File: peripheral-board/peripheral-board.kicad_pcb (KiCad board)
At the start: 2 copper layers, 165 x 100 mm, 144 parts, among them IC1001 ATTINY48-A, SW2001 1, SW2002 2, SW2003 3, SW2004 4, SW2005 5, SW2006 6, SW2007 7, SW2008 8, SW2009 9, SW2010 0, SW2011 1, SW2012 2, SW2013 3, SW2014 4, SW2015 5, SW2016 6, SW2017 7, SW2018 8, SW2019 9, SW2020 0, SW2021 Q, SW2022 W, SW2023 E, SW2024 R, SW2025 T, SW2026 Y, SW2027 U, SW2028 I, SW2029 O, SW2030 P, SW2031 Q, SW2032 W, SW2033 E, SW2034 R, SW2035 T, SW2036 Y, SW2037 U, SW2038 I, SW2039 O, SW2040 P, SW2041 A, SW2042 S, SW2043 D, SW2044 F, SW2045 G, SW2046 H, SW2047 J, SW2048 K, SW2049 L, SW2050 Ö, SW2051 A, SW2052 S, SW2053 D, SW2054 F, SW2055 G, SW2056 H, SW2057 J, SW2058 K, SW2059 L, SW2060 Ö, SW2061 Z, SW2062 X, SW2063 C, SW2064 V, SW2065 B, SW2066 N, SW2067 M, SW2068 ,, SW2069 ., SW2070 -, SW3001 Left, SW3002 MIddle, SW3003 Right

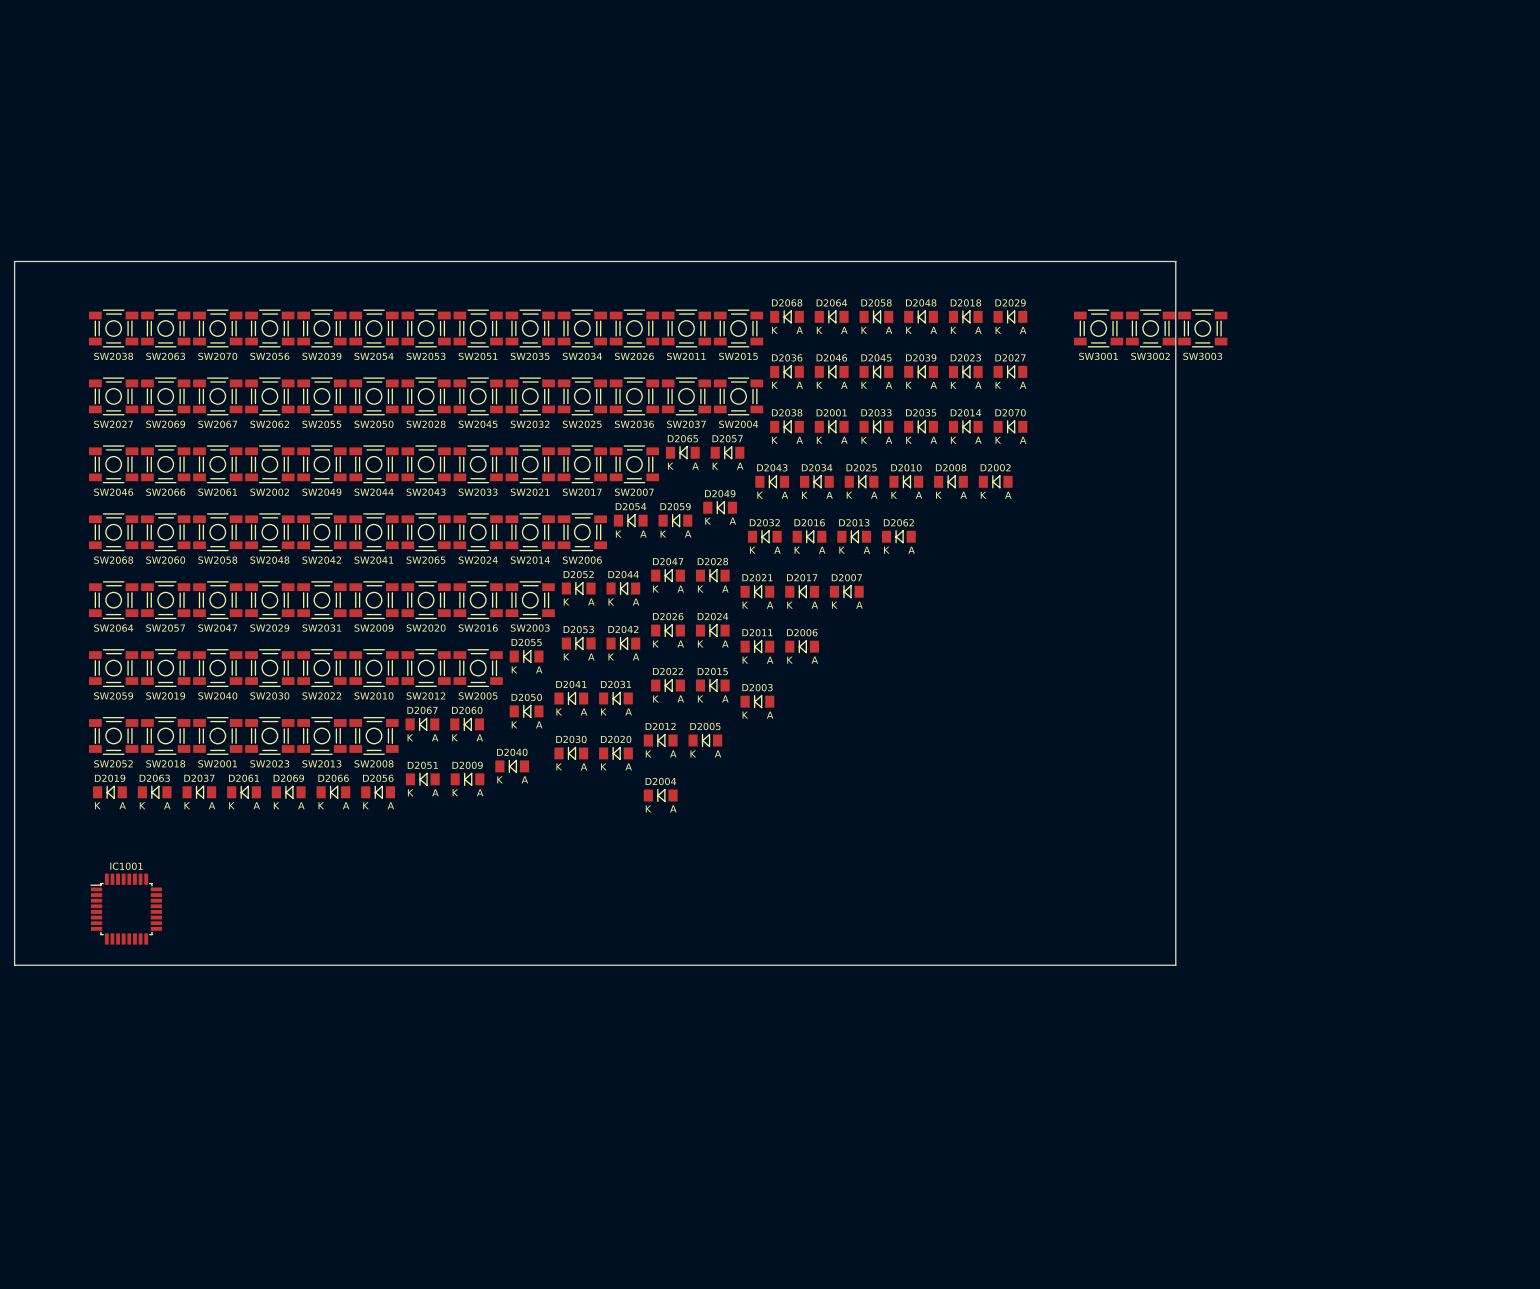
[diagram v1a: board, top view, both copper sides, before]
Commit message: added keyboard scanning logic
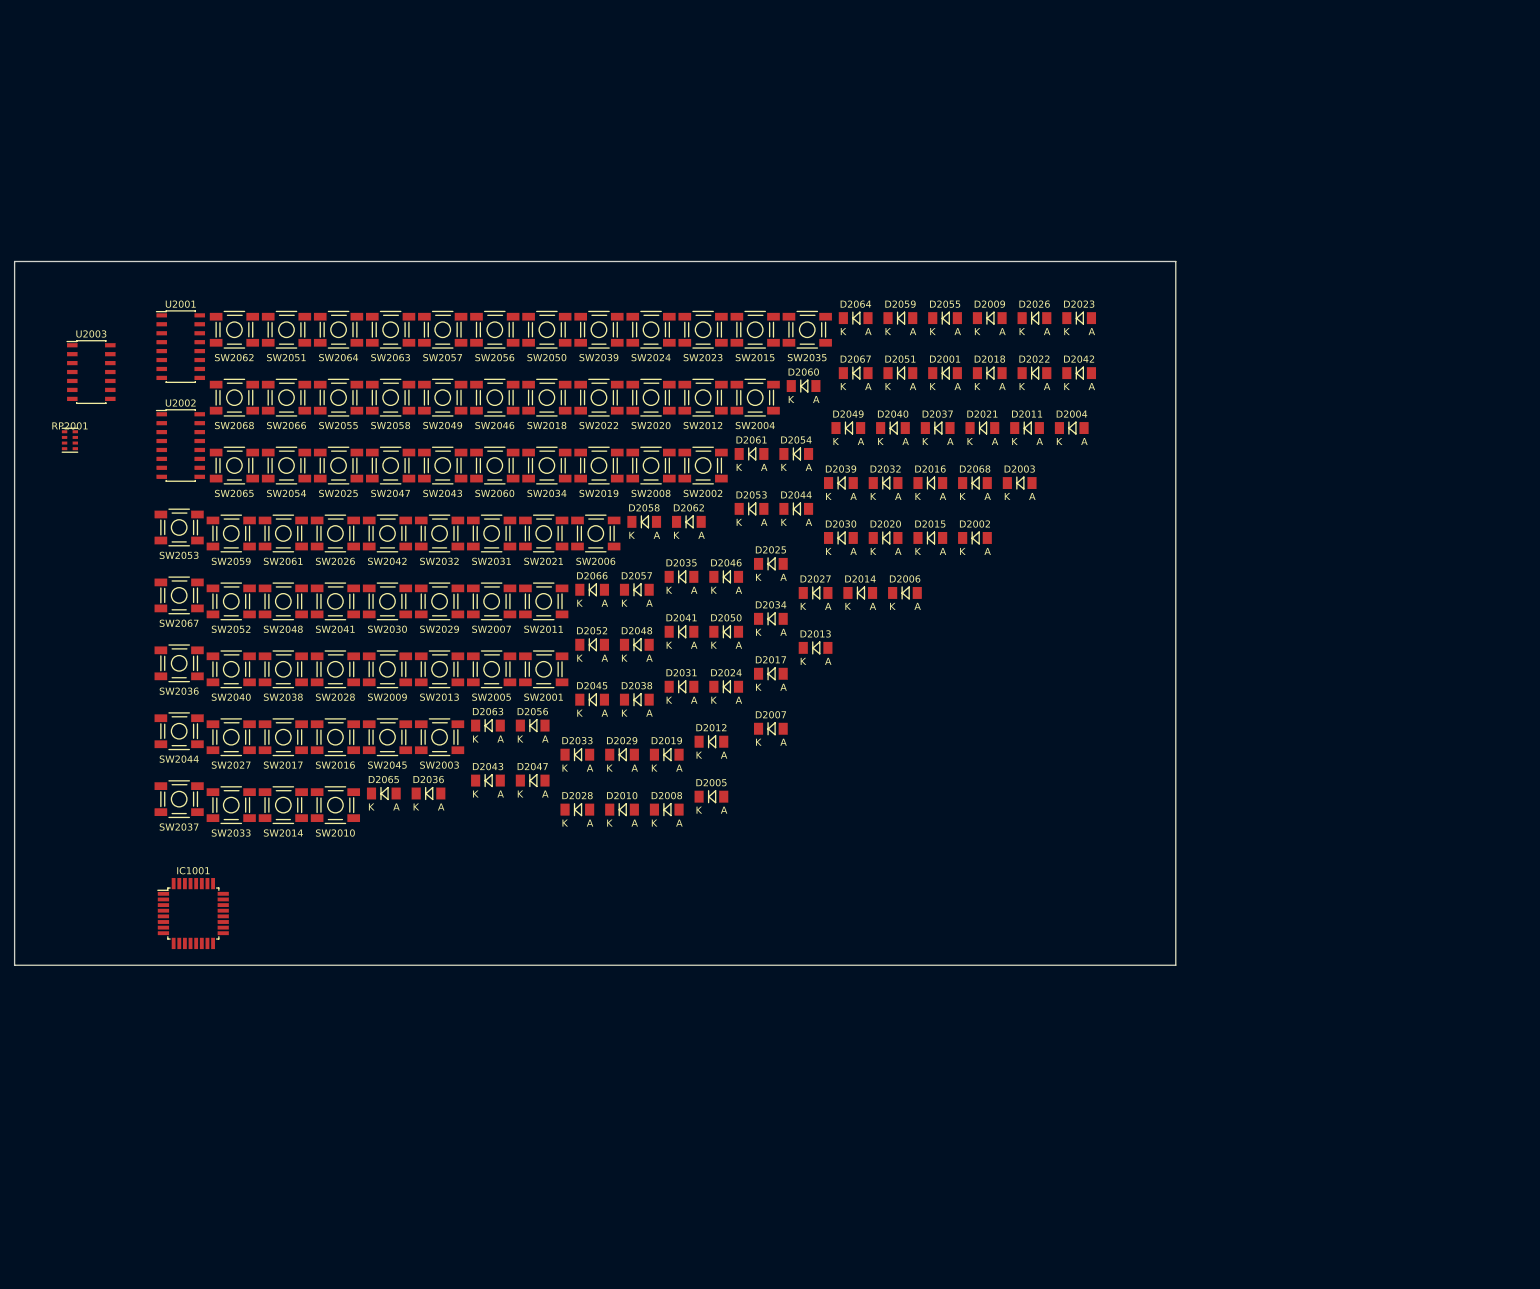
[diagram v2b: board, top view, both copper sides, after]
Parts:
- removed D2069, D2070: 1N4148, Diodes_SMD:MiniMELF_Standard
- removed SW2069: ., lib:SMD-TACT-5.2x5.2x2mm
- removed SW2070: -, lib:SMD-TACT-5.2x5.2x2mm
- removed SW3001: Left, lib:SMD-TACT-5.2x5.2x2mm
- removed SW3002: MIddle, lib:SMD-TACT-5.2x5.2x2mm
- removed SW3003: Right, lib:SMD-TACT-5.2x5.2x2mm
- added RP2001: 10k, Resistors_SMD:R_Cat16-4, F.Cu at (67.9, 70.4)
- added U2001: 4017, Housings_SOIC:SOIC-16_3.9x9.9mm_Pitch1.27mm, F.Cu at (83.6, 57.1)
- added U2002: 4017, Housings_SOIC:SOIC-16_3.9x9.9mm_Pitch1.27mm, F.Cu at (83.6, 71.1)
- added U2003: 74HC00, Housings_SOIC:SOIC-14_3.9x8.7mm_Pitch1.27mm, F.Cu at (70.9, 60.7)
- SW2011: value 1 -> +
- SW2012: value 2 -> ´
- SW2013: value 3 -> BKSP
- SW2014: value 4 -> TROLL
- SW2015: value 5 -> §
- SW2016: value 6 -> UP
- SW2017: value 7 -> RMB
- SW2018: value 8 -> Q
- SW2019: value 9 -> W
- SW2020: value 0 -> E
- SW2021: value Q -> R
- SW2022: value W -> T
- SW2023: value E -> Y
- SW2024: value R -> U
- SW2025: value T -> I
- SW2026: value Y -> O
- SW2027: value U -> P
- SW2028: value I -> Å
- SW2029: value O -> ¨
- SW2030: value P -> RETURN
- SW2031: value Q -> ALT_GR
- SW2032: value W -> <
- SW2033: value E -> LEFT
- SW2034: value R -> MMB
- SW2035: value T -> A
- SW2036: value Y -> S
- SW2037: value U -> D
- SW2038: value I -> F
- SW2039: value O -> G
- SW2040: value P -> H
- SW2041: value A -> J
- SW2042: value S -> K
- SW2043: value D -> L
- SW2044: value F -> Ö
- SW2045: value G -> Ä
- SW2046: value H -> '
- SW2047: value J -> ESC
- SW2048: value K -> TAB
- SW2049: value L -> ALT
- SW2050: value Ö -> DOWN
- SW2051: value A -> LMB
- SW2052: value S -> SHIFT_L
- SW2053: value D -> Z
- SW2054: value F -> X
- SW2055: value G -> C
- SW2056: value H -> V
- SW2057: value J -> B
- SW2058: value K -> N
- SW2059: value L -> M
- SW2060: value Ö -> ,
- SW2061: value Z -> .
- SW2062: value X -> -
- SW2063: value C -> SHIFT_R
- SW2064: value V -> FN_R
- SW2065: value B -> SPACE
- SW2066: value N -> FN_L
- SW2067: value M -> RIGHT
- SW2068: value , -> CTRL
- moved D2037 117.0 mm to (191.2, 68.7)
- moved D2009 99.0 mm to (198.6, 53.0)
- moved SW2037 92.0 mm to (83.4, 121.4)
- moved D2051 89.1 mm to (185.9, 60.9)
- moved D2061 86.7 mm to (164.7, 72.3)
- moved SW2023 84.4 mm to (157.8, 54.7)
- moved D2029 83.2 mm to (146.3, 115.1)
- moved D2019 79.3 mm to (152.7, 115.1)
- moved D2067 79.3 mm to (179.5, 60.9)
- moved D2036 78.6 mm to (118.8, 120.6)
- moved D2004 78.3 mm to (210.2, 68.7)
- moved D2055 76.5 mm to (192.2, 53.0)
- moved D2042 75.3 mm to (211.3, 60.9)
- moved SW2036 75.0 mm to (83.4, 102.1)
- moved SW2018 72.4 mm to (135.6, 64.3)
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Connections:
- D2001 pad 1: Net-(D2001-Pad1) -> /Keyboard/Q0
- D2002 pad 1: Net-(D2001-Pad1) -> /Keyboard/Q0
- D2003 pad 1: Net-(D2001-Pad1) -> /Keyboard/Q0
- D2004 pad 1: Net-(D2001-Pad1) -> /Keyboard/Q0
- D2005 pad 1: Net-(D2001-Pad1) -> /Keyboard/Q0
- D2006 pad 1: Net-(D2001-Pad1) -> /Keyboard/Q0
- D2007 pad 1: Net-(D2001-Pad1) -> /Keyboard/Q0
- D2008 pad 1: Net-(D2001-Pad1) -> /Keyboard/Q0
- D2009 pad 1: Net-(D2001-Pad1) -> /Keyboard/Q0
- D2010 pad 1: Net-(D2001-Pad1) -> /Keyboard/Q0
- D2011 pad 1: Net-(D2011-Pad1) -> /Keyboard/Q0
- D2012 pad 1: Net-(D2011-Pad1) -> /Keyboard/Q0
- D2013 pad 1: Net-(D2011-Pad1) -> /Keyboard/Q0
- D2014 pad 1: Net-(D2011-Pad1) -> /Keyboard/Q0
- D2015 pad 1: Net-(D2011-Pad1) -> /Keyboard/Q0
- D2016 pad 1: Net-(D2011-Pad1) -> /Keyboard/Q0
- D2017 pad 1: Net-(D2011-Pad1) -> /Keyboard/Q0
- D2018 pad 1: Net-(D2011-Pad1) -> /Keyboard/Q1
- D2019 pad 1: Net-(D2011-Pad1) -> /Keyboard/Q1
- D2020 pad 1: Net-(D2011-Pad1) -> /Keyboard/Q1
- D2021 pad 1: Net-(D2021-Pad1) -> /Keyboard/Q1
- D2022 pad 1: Net-(D2021-Pad1) -> /Keyboard/Q1
- D2023 pad 1: Net-(D2021-Pad1) -> /Keyboard/Q1
- D2024 pad 1: Net-(D2021-Pad1) -> /Keyboard/Q1
- D2025 pad 1: Net-(D2021-Pad1) -> /Keyboard/Q1
- D2026 pad 1: Net-(D2021-Pad1) -> /Keyboard/Q1
- D2027 pad 1: Net-(D2021-Pad1) -> /Keyboard/Q1
- D2028 pad 1: Net-(D2021-Pad1) -> /Keyboard/Q1
- D2029 pad 1: Net-(D2021-Pad1) -> /Keyboard/Q1
- D2030 pad 1: Net-(D2021-Pad1) -> /Keyboard/Q1
- D2031 pad 1: Net-(D2031-Pad1) -> /Keyboard/Q1
- D2032 pad 1: Net-(D2031-Pad1) -> /Keyboard/Q1
- D2033 pad 1: Net-(D2031-Pad1) -> /Keyboard/Q1
- D2034 pad 1: Net-(D2031-Pad1) -> /Keyboard/Q1
- D2035 pad 1: Net-(D2031-Pad1) -> /Keyboard/Q2
- D2036 pad 1: Net-(D2031-Pad1) -> /Keyboard/Q2
- D2037 pad 1: Net-(D2031-Pad1) -> /Keyboard/Q2
- D2038 pad 1: Net-(D2031-Pad1) -> /Keyboard/Q2
- D2039 pad 1: Net-(D2031-Pad1) -> /Keyboard/Q2
- D2040 pad 1: Net-(D2031-Pad1) -> /Keyboard/Q2
- D2041 pad 1: Net-(D2041-Pad1) -> /Keyboard/Q2
- D2042 pad 1: Net-(D2041-Pad1) -> /Keyboard/Q2
- D2043 pad 1: Net-(D2041-Pad1) -> /Keyboard/Q2
- D2044 pad 1: Net-(D2041-Pad1) -> /Keyboard/Q2
- D2045 pad 1: Net-(D2041-Pad1) -> /Keyboard/Q2
- D2046 pad 1: Net-(D2041-Pad1) -> /Keyboard/Q2
- D2047 pad 1: Net-(D2041-Pad1) -> /Keyboard/Q2
- D2048 pad 1: Net-(D2041-Pad1) -> /Keyboard/Q2
- D2049 pad 1: Net-(D2041-Pad1) -> /Keyboard/Q2
- D2050 pad 1: Net-(D2041-Pad1) -> /Keyboard/Q2
- D2051 pad 1: Net-(D2051-Pad1) -> /Keyboard/Q2
- D2052 pad 1: Net-(D2051-Pad1) -> /Keyboard/Q3
- D2053 pad 1: Net-(D2051-Pad1) -> /Keyboard/Q3
- D2054 pad 1: Net-(D2051-Pad1) -> /Keyboard/Q3
- D2055 pad 1: Net-(D2051-Pad1) -> /Keyboard/Q3
- D2056 pad 1: Net-(D2051-Pad1) -> /Keyboard/Q3
- D2057 pad 1: Net-(D2051-Pad1) -> /Keyboard/Q3
- D2058 pad 1: Net-(D2051-Pad1) -> /Keyboard/Q3
- D2059 pad 1: Net-(D2051-Pad1) -> /Keyboard/Q3
- D2060 pad 1: Net-(D2051-Pad1) -> /Keyboard/Q3
- D2061 pad 1: Net-(D2061-Pad1) -> /Keyboard/Q3
- D2062 pad 1: Net-(D2061-Pad1) -> /Keyboard/Q3
- D2063 pad 1: Net-(D2061-Pad1) -> /Keyboard/Q3
- D2064 pad 1: Net-(D2061-Pad1) -> /Keyboard/Q3
- D2065 pad 1: Net-(D2061-Pad1) -> /Keyboard/Q3
- D2066 pad 1: Net-(D2061-Pad1) -> /Keyboard/Q3
- D2067 pad 1: Net-(D2061-Pad1) -> /Keyboard/Q3
- D2068 pad 1: Net-(D2061-Pad1) -> /Keyboard/Q3
- SW2018 pad 1: Net-(SW2018-Pad1) -> Net-(SW2001-Pad1)
- SW2019 pad 1: Net-(SW2019-Pad1) -> Net-(SW2002-Pad1)
- SW2020 pad 1: Net-(SW2020-Pad1) -> Net-(SW2003-Pad1)
- SW2021 pad 1: Net-(SW2001-Pad1) -> Net-(SW2004-Pad1)
- SW2022 pad 1: Net-(SW2002-Pad1) -> Net-(SW2005-Pad1)
- SW2023 pad 1: Net-(SW2003-Pad1) -> Net-(SW2006-Pad1)
- SW2024 pad 1: Net-(SW2004-Pad1) -> Net-(SW2007-Pad1)
- SW2025 pad 1: Net-(SW2005-Pad1) -> Net-(SW2008-Pad1)
- SW2026 pad 1: Net-(SW2006-Pad1) -> Net-(SW2009-Pad1)
- SW2027 pad 1: Net-(SW2007-Pad1) -> Net-(SW2010-Pad1)
- SW2028 pad 1: Net-(SW2008-Pad1) -> Net-(SW2011-Pad1)
- SW2029 pad 1: Net-(SW2029-Pad1) -> Net-(SW2012-Pad1)
- SW2030 pad 1: Net-(SW2010-Pad1) -> Net-(SW2013-Pad1)
- SW2031 pad 1: Net-(SW2011-Pad1) -> Net-(SW2014-Pad1)
- SW2032 pad 1: Net-(SW2012-Pad1) -> Net-(SW2015-Pad1)
- SW2033 pad 1: Net-(SW2013-Pad1) -> Net-(SW2016-Pad1)
- SW2034 pad 1: Net-(SW2014-Pad1) -> Net-(SW2017-Pad1)
- SW2035 pad 1: Net-(SW2015-Pad1) -> Net-(SW2001-Pad1)
- SW2036 pad 1: Net-(SW2016-Pad1) -> Net-(SW2002-Pad1)
- SW2037 pad 1: Net-(SW2017-Pad1) -> Net-(SW2003-Pad1)
- SW2038 pad 1: Net-(SW2018-Pad1) -> Net-(SW2004-Pad1)
- SW2039 pad 1: Net-(SW2039-Pad1) -> Net-(SW2005-Pad1)
- SW2040 pad 1: Net-(SW2020-Pad1) -> Net-(SW2006-Pad1)
- SW2041 pad 1: Net-(SW2001-Pad1) -> Net-(SW2007-Pad1)
- SW2042 pad 1: Net-(SW2002-Pad1) -> Net-(SW2008-Pad1)
- SW2043 pad 1: Net-(SW2003-Pad1) -> Net-(SW2009-Pad1)
- SW2044 pad 1: Net-(SW2004-Pad1) -> Net-(SW2010-Pad1)
- SW2045 pad 1: Net-(SW2005-Pad1) -> Net-(SW2011-Pad1)
- SW2046 pad 1: Net-(SW2006-Pad1) -> Net-(SW2012-Pad1)
- SW2047 pad 1: Net-(SW2007-Pad1) -> Net-(SW2013-Pad1)
- SW2048 pad 1: Net-(SW2008-Pad1) -> Net-(SW2014-Pad1)
- SW2049 pad 1: Net-(SW2029-Pad1) -> Net-(SW2015-Pad1)
- SW2050 pad 1: Net-(SW2010-Pad1) -> Net-(SW2016-Pad1)
- SW2051 pad 1: Net-(SW2011-Pad1) -> Net-(SW2017-Pad1)
- SW2052 pad 1: Net-(SW2012-Pad1) -> Net-(SW2001-Pad1)
- SW2052 pad 2: Net-(D2052-Pad2) -> Net-(D2059-Pad2)
- SW2053 pad 1: Net-(SW2013-Pad1) -> Net-(SW2002-Pad1)
- SW2053 pad 2: Net-(D2053-Pad2) -> Net-(D2060-Pad2)
- SW2054 pad 1: Net-(SW2014-Pad1) -> Net-(SW2003-Pad1)
- SW2054 pad 2: Net-(D2054-Pad2) -> Net-(D2061-Pad2)
- SW2055 pad 1: Net-(SW2015-Pad1) -> Net-(SW2004-Pad1)
- SW2055 pad 2: Net-(D2055-Pad2) -> Net-(D2062-Pad2)
- SW2056 pad 1: Net-(SW2016-Pad1) -> Net-(SW2005-Pad1)
- SW2056 pad 2: Net-(D2056-Pad2) -> Net-(D2063-Pad2)
- SW2057 pad 1: Net-(SW2017-Pad1) -> Net-(SW2006-Pad1)
- SW2057 pad 2: Net-(D2057-Pad2) -> Net-(D2064-Pad2)
- SW2058 pad 1: Net-(SW2018-Pad1) -> Net-(SW2007-Pad1)
- SW2058 pad 2: Net-(D2058-Pad2) -> Net-(D2065-Pad2)
- SW2059 pad 1: Net-(SW2039-Pad1) -> Net-(SW2008-Pad1)
- SW2059 pad 2: Net-(D2059-Pad2) -> Net-(D2066-Pad2)
- SW2060 pad 1: Net-(SW2020-Pad1) -> Net-(SW2009-Pad1)
- SW2060 pad 2: Net-(D2060-Pad2) -> Net-(D2067-Pad2)
- SW2061 pad 1: Net-(SW2001-Pad1) -> Net-(SW2010-Pad1)
- SW2061 pad 2: Net-(D2061-Pad2) -> Net-(D2068-Pad2)
- SW2062 pad 1: Net-(SW2002-Pad1) -> Net-(SW2011-Pad1)
- SW2062 pad 2: Net-(D2062-Pad2) -> Net-(D2052-Pad2)
- SW2063 pad 1: Net-(SW2003-Pad1) -> Net-(SW2012-Pad1)
- SW2063 pad 2: Net-(D2063-Pad2) -> Net-(D2053-Pad2)
- SW2064 pad 1: Net-(SW2004-Pad1) -> Net-(SW2013-Pad1)
- SW2064 pad 2: Net-(D2064-Pad2) -> Net-(D2054-Pad2)
- SW2065 pad 1: Net-(SW2005-Pad1) -> Net-(SW2014-Pad1)
- SW2065 pad 2: Net-(D2065-Pad2) -> Net-(D2055-Pad2)
- SW2066 pad 1: Net-(SW2006-Pad1) -> Net-(SW2015-Pad1)
- SW2066 pad 2: Net-(D2066-Pad2) -> Net-(D2056-Pad2)
- SW2067 pad 1: Net-(SW2007-Pad1) -> Net-(SW2016-Pad1)
- SW2067 pad 2: Net-(D2067-Pad2) -> Net-(D2057-Pad2)
- SW2068 pad 1: Net-(SW2008-Pad1) -> Net-(SW2017-Pad1)
- SW2068 pad 2: Net-(D2068-Pad2) -> Net-(D2058-Pad2)

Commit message: added peripheral board bus header
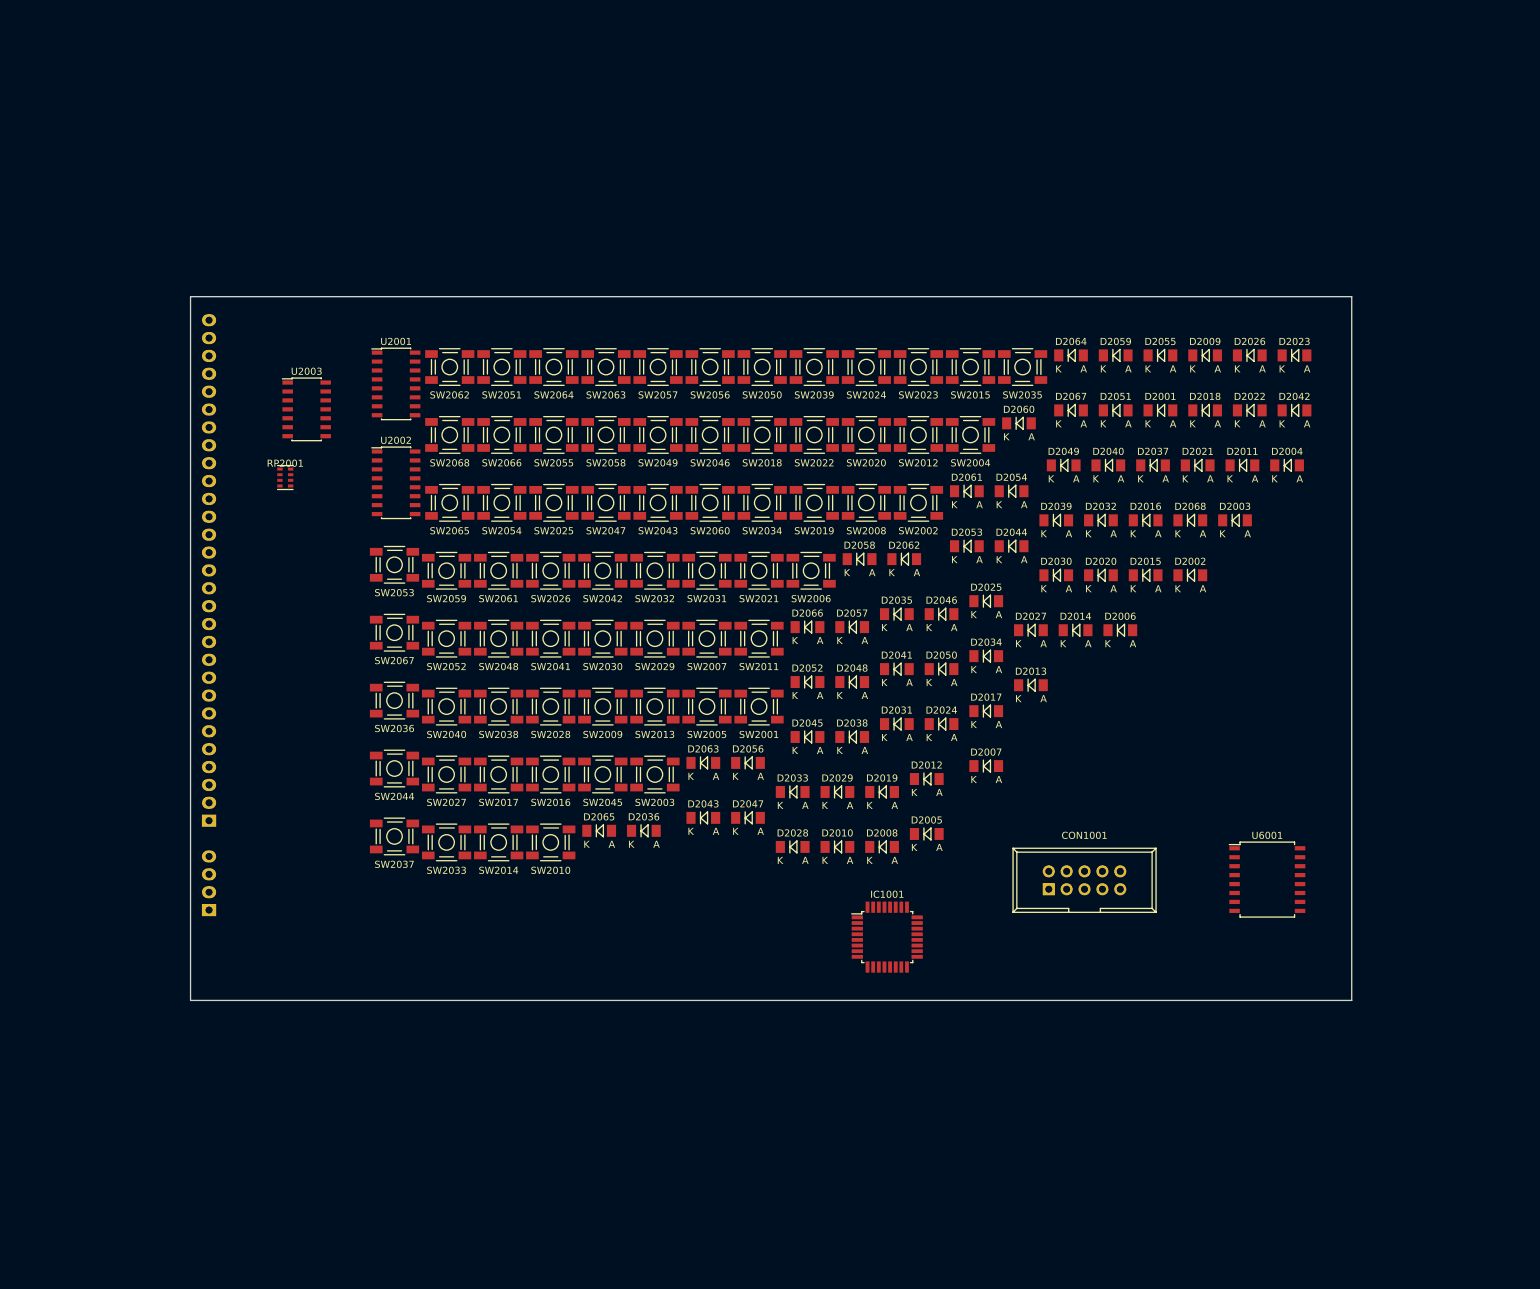
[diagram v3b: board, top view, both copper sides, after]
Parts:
- added CON1001: AVR-ISP-10, Connect:IDC_Header_Straight_10pins, F.Cu at (207.0, 134.2)
- added P1001: Peripheral Bus, Socket_Strips:Socket_Strip_Straight_1x29, B.Cu at (87.6, 124.5)
- added P1002: Power, Socket_Strips:Socket_Strip_Straight_1x04, B.Cu at (87.6, 137.2)
- added U6001: TCA0372, Housings_SOIC:SOIC-16_7.5x10.3mm_Pitch1.27mm, F.Cu at (238.0, 132.8)
- moved IC1001 98.7 mm to (184.0, 141.0)
- moved D2003 31.1 mm to (233.4, 81.8)
- moved SW2001 31.1 mm to (165.8, 108.2)
- moved D2009 31.1 mm to (229.2, 58.3)
- moved D2010 31.1 mm to (176.9, 128.2)
- moved D2013 31.1 mm to (204.4, 105.2)
- moved D2018 31.1 mm to (229.2, 66.2)
- moved D2027 31.1 mm to (204.4, 97.4)
- moved D2029 31.1 mm to (176.9, 120.4)
- moved D2040 31.1 mm to (215.4, 74.0)
- moved D2044 31.1 mm to (201.7, 85.5)
- moved D2045 31.1 mm to (172.7, 112.6)
- moved D2052 31.1 mm to (172.7, 104.8)
- moved D2054 31.1 mm to (201.7, 77.6)
- moved D2062 31.1 mm to (186.4, 87.3)
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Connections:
- IC1001 pad 21: Net-(IC1001-Pad21) -> GND
- IC1001 pad 5: Net-(IC1001-Pad5) -> GND
